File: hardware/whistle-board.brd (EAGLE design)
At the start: 75.9 x 21.7 mm, 17 parts, among them IC1 MCP4131, IC2 L272, Q1 BC638, Q3 BC638

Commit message: revisions after the most recent draft was assembled and tested
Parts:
- removed Q3: BC638, custom-parts:TO-92
- removed R5: 1k, SparkFun-Resistors:AXIAL-0.3
- removed SERIAL: (no value), SparkFun-Connectors:1X03
- AUX: device SparkFun-Connectors:1X03 -> SparkFun-Connectors:1X02
- CTL: device SparkFun-Connectors:1X02 -> SparkFun-Connectors:1X04
- Q1: value BC638 -> (none)
- moved Q1 20.8 mm to (47.0, 14.0), turned to 90 degrees
- moved CTL 16.6 mm to (29.2, 17.1)
- moved TRACK 2.54 mm to (62.2, 17.1)
- moved S1 2.54 mm to (57.9, 10.0)
- moved AUX 2.04 mm to (54.6, 17.1)
- moved POW 2.04 mm to (39.4, 17.1)
- moved IC2 1.27 mm to (34.0, 6.03)
- moved R4 0.38 mm to (37.1, 13.1)
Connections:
- removed net 12V-EN: AUX.3, IC2.V+, Q1.3
- removed net EN: CTL.2, R4.P$1
- removed net N$5: Q3.2, R5.P$1
- net 12V: now also IC2.V+; no longer Q1.1
- net 5V: now also D1.C, S1.+; no longer Q3.1
- net CS: now also CTL.2; no longer SERIAL.1
- net DIR: now also R4.P$2; no longer R5.P$2
- net GND: now also Q1.1; no longer S1.-
- net N$1: now also Q1.3, S1.-; no longer Q1.2, R4.P$2
- net N$2: now also Q1.2, R4.P$1; no longer D1.C, Q3.3, S1.+
- net SCK: now also CTL.3; no longer SERIAL.2
- net SDI: now also CTL.4; no longer SERIAL.3
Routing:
- net 12V-EN: track 30.0 -> 0.00 mm
- net 5V: track 0.00 -> 9.44 mm
- net POW: track 38.7 -> 46.0 mm
- net EN: track 5.19 -> 0.00 mm
- net 12V: track 14.1 -> 9.00 mm
- net N$5: track 4.73 -> 0.00 mm
- net N$2: track 8.67 -> 4.56 mm
- net WIPER: track 22.5 -> 21.2 mm
- net N$3: track 6.89 -> 8.16 mm
- net LEFT: track 11.9 -> 12.8 mm
- net DIR: track 5.04 -> 5.72 mm
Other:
- board text added: "2N 3904"
- board text added: "black"
- board text added: "blue"
- board text added: "brown"
- board text added: "green"
- board text added: "orange"
- board text added: "purple"
- board text added: "red"
- board text added: "yellow"
- board text removed: "BC638"

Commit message: sloppily terminating unused opamp
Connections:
- net GND: now also IC2.IN2+, IC2.IN2-
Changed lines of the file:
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@@
 <contactref element="Q1" pad="1"/>
 <contactref element="AUX" pad="2"/>
+<contactref element="IC2" pad="IN2+"/>
+<contactref element="IC2" pad="IN2-"/>
 </signal>
 <signal name="12V">

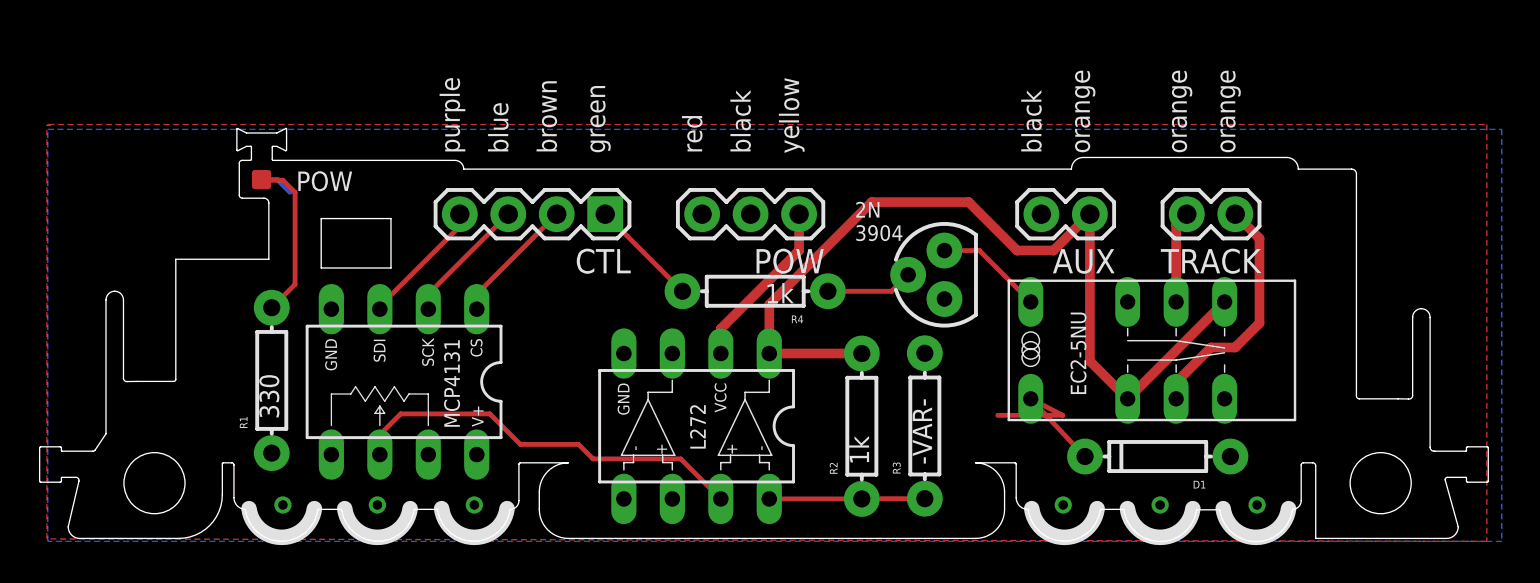
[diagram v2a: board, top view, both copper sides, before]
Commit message: adding/fixing diodes, adding silkscreen details
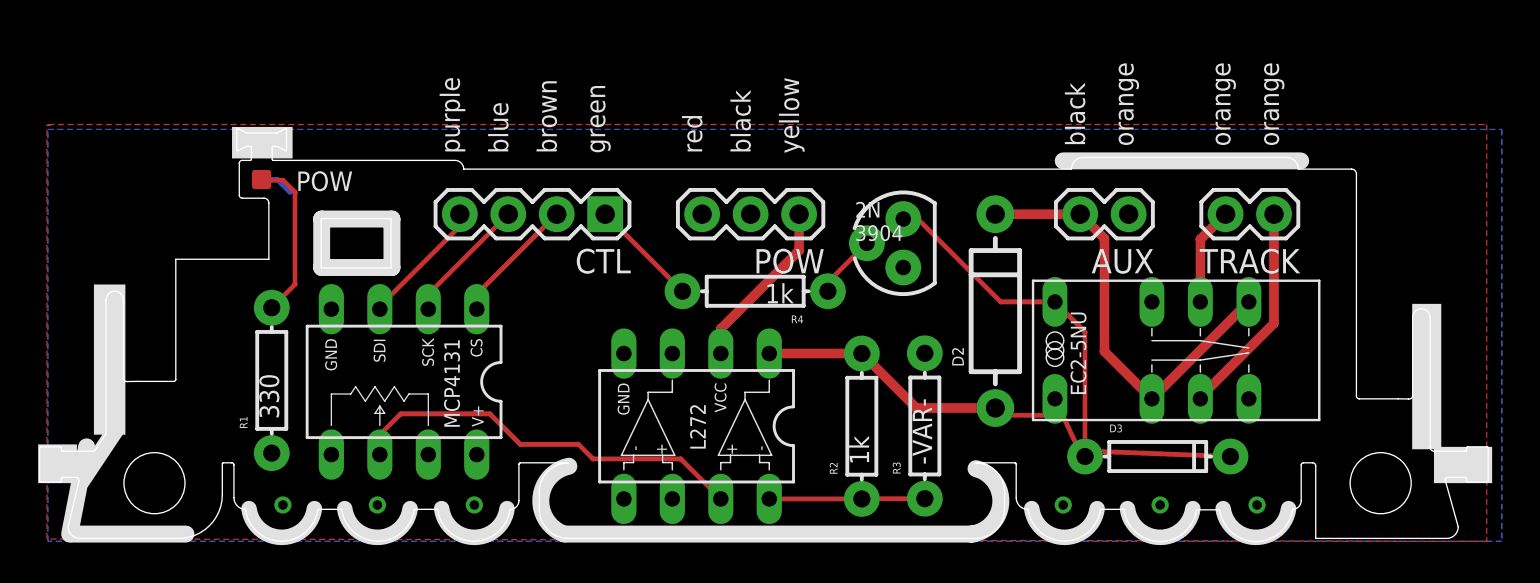
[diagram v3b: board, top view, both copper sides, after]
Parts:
- added D3: (no value), SparkFun-DiscreteSemi:DIODE-1N4148
- D1: value (none) -> Yellow; device SparkFun-DiscreteSemi:DIODE-1N4148 -> custom-parts:LED-EDGE
- D2: value Yellow -> (none); device custom-parts:LED-EDGE -> SparkFun-DiscreteSemi:DIODE-1N4001
- moved D1 49.2 mm to (11.2, 18.9), flipped to the bottom, turned to 0 degrees
- moved D2 39.1 mm to (49.7, 12.1), flipped to the top, turned to 90 degrees
- moved Q1 2.72 mm to (44.8, 15.6)
- moved AUX 2.03 mm to (56.6, 17.1)
- moved TRACK 2.03 mm to (64.3, 17.1)
- moved S1 1.27 mm to (59.1, 10.0)
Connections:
- new net N$5: D2.A, IC2.OUT1, R2.P$2
- net 5V: now also D3.C; no longer D1.C
- net GND: now also AUX.1, D1.C; no longer AUX.2, D1.A, D2.C
- net N$1: now also D3.A
- net N$19: now also D1.A; no longer D2.A
- net POW: now also AUX.2, D2.C; no longer AUX.1, IC2.OUT1, R2.P$2
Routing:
- net POW: track 46.0 -> 22.9 mm
- net N$5: track 0.00 -> 13.0 mm
- net N$1: track 5.64 -> 18.5 mm
- net 5V: track 9.44 -> 15.3 mm
- net LEFT: track 12.8 -> 11.3 mm
- net N$2: track 4.56 -> 3.36 mm

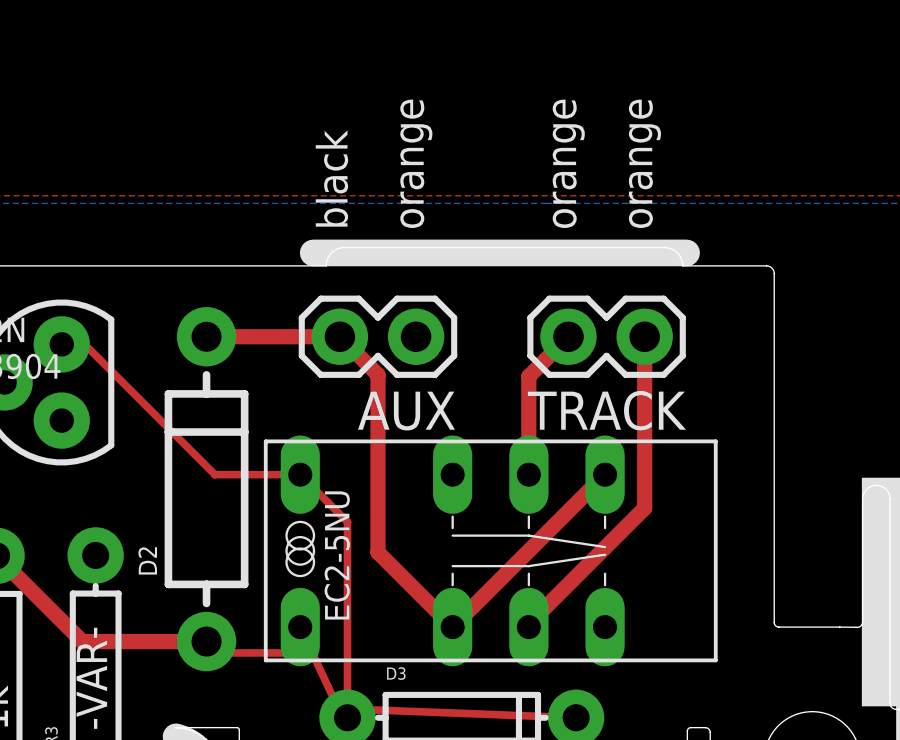
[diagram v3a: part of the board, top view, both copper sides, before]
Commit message: 0.1 pin spacing
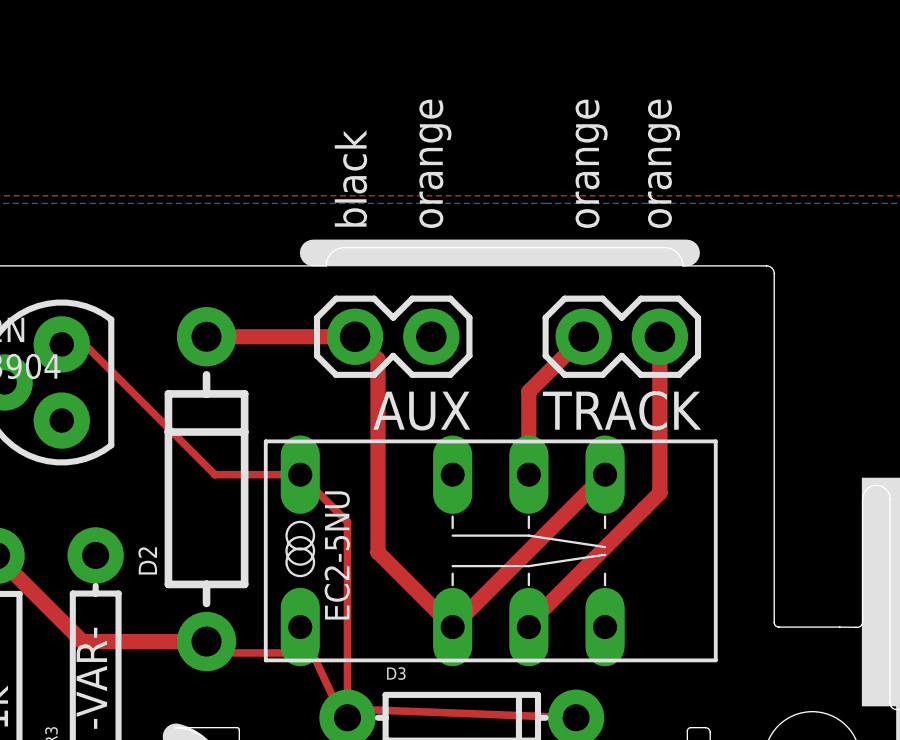
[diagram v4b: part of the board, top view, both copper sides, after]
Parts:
- moved AUX 0.51 mm to (57.1, 17.1)
- moved TRACK 0.51 mm to (64.8, 17.1)
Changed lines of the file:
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@@
 <text x="26.67" y="20.32" size="1.016" layer="25" rot="R90">brown</text>
 <text x="29.21" y="20.32" size="1.016" layer="25" rot="R90">green</text>
-<text x="61.976" y="20.701" size="1.016" layer="25" rot="R90">orange</text>
-<text x="64.516" y="20.701" size="1.016" layer="25" rot="R90">orange</text>
-<text x="54.356" y="20.701" size="1.016" layer="25" rot="R90">black</text>
-<text x="56.896" y="20.701" size="1.016" layer="25" rot="R90">orange</text>
+<text x="62.738" y="20.701" size="1.016" layer="25" rot="R90">orange</text>
+<text x="65.151" y="20.701" size="1.016" layer="25" rot="R90">orange</text>
+<text x="54.991" y="20.701" size="1.016" layer="25" rot="R90">black</text>
+<text x="57.531" y="20.701" size="1.016" layer="25" rot="R90">orange</text>
 <text x="42.291" y="15.748" size="0.8128" layer="21">2N
 3904</text>
@@
 </element>
 <element name="D3" library="SparkFun-DiscreteSemi" package="DIODE-1N4148" value="" x="58.166" y="4.445"/>
-<element name="TRACK" library="SparkFun-Connectors" package="1X02" value="" x="64.262" y="17.145" rot="R180"/>
+<element name="TRACK" library="SparkFun-Connectors" package="1X02" value="" x="64.77" y="17.145" rot="R180"/>
 <element name="POW" library="SparkFun-Connectors" package="1X03" value="" x="39.37" y="17.145" rot="R180"/>
 <element name="Q1" library="custom-parts" package="TO-92" value="" x="44.831" y="15.621" rot="R90"/>
 <element name="CTL" library="SparkFun-Connectors" package="1X04" value="" x="29.21" y="17.145" rot="R180"/>
-<element name="AUX" library="SparkFun-Connectors" package="1X02" value="" x="56.642" y="17.145" rot="R180"/>
+<element name="AUX" library="SparkFun-Connectors" package="1X02" value="" x="57.15" y="17.145" rot="R180"/>
 <element name="D2" library="SparkFun-DiscreteSemi" package="DIODE-1N4001" value="" x="49.657" y="12.065" rot="R90"/>
 </elements>
@@
 <contactref element="D2" pad="C"/>
 <contactref element="AUX" pad="2"/>
-<wire x1="54.102" y1="17.145" x2="55.372" y2="15.875" width="0.508" layer="1"/>
-<wire x1="55.372" y1="15.875" x2="55.372" y2="9.9568" width="0.508" layer="1"/>
 <wire x1="55.372" y1="9.9568" x2="57.8612" y2="7.4676" width="0.508" layer="1"/>
 <wire x1="57.8612" y1="7.4676" x2="62.9412" y2="12.5476" width="0.508" layer="1"/>
-<wire x1="49.657" y1="17.145" x2="54.102" y2="17.145" width="0.508" layer="1"/>
+<wire x1="49.657" y1="17.145" x2="54.61" y2="17.145" width="0.508" layer="1"/>
+<wire x1="55.372" y1="9.9568" x2="55.372" y2="16.383" width="0.508" layer="1"/>
+<wire x1="55.372" y1="16.383" x2="54.61" y2="17.145" width="0.508" layer="1"/>
 </signal>
 <signal name="DIR">
@@
 <wire x1="60.4012" y1="7.4676" x2="60.4012" y2="7.5692" width="0.4064" layer="1"/>
 <wire x1="60.4012" y1="7.5692" x2="64.262" y2="11.43" width="0.508" layer="1"/>
-<wire x1="64.262" y1="11.43" x2="64.262" y2="17.145" width="0.508" layer="1"/>
+<wire x1="64.262" y1="11.43" x2="64.77" y2="11.938" width="0.508" layer="1"/>
+<wire x1="64.77" y1="11.938" x2="64.77" y2="17.145" width="0.508" layer="1"/>
 </signal>
 <signal name="RIGHT">
 <contactref element="S1" pad="COM2"/>
 <contactref element="TRACK" pad="2"/>
-<wire x1="60.4012" y1="12.5476" x2="60.4012" y2="15.8242" width="0.508" layer="1"/>
-<wire x1="60.4012" y1="15.8242" x2="61.722" y2="17.145" width="0.508" layer="1"/>
+<wire x1="60.4012" y1="12.5476" x2="60.4012" y2="15.3162" width="0.508" layer="1"/>
+<wire x1="60.4012" y1="15.3162" x2="62.23" y2="17.145" width="0.508" layer="1"/>
 </signal>
 <signal name="N$4">
